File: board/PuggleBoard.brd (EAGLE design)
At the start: 54.6 x 86.4 mm, 133 parts, among them U1 LMP7704, U10 SN65LVDS2, U11 SN65LVDS1, U12 SN65LVDS1, U13 SN65LVDS1, U14 SN65MLVD201D, U15 24C, U2 ADS8331, U3 OPA4209, U4 AD5686, U5 LTM8045, U6 TPS7A3001, U7 TPS7A4901, U8 REF5040, U9 AD8032

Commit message: A few minor changes.
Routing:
- net VDRIVE: track 36.6 -> 45.9 mm
- net SPI4: track 9.88 -> 17.7 mm
- net MISO1_N: track 17.8 -> 19.3 mm
- net MISO1_P: track 21.8 -> 23.2 mm
- net GND: track 115.6 -> 116.4 mm
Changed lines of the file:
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@@
 <layers>
 <layer number="1" name="Top" color="12" fill="1" visible="yes" active="yes"/>
-<layer number="2" name="GND" color="12" fill="3" visible="no" active="yes"/>
+<layer number="2" name="GND" color="12" fill="3" visible="yes" active="yes"/>
 <layer number="3" name="Route3" color="4" fill="3" visible="no" active="no"/>
 <layer number="4" name="Route4" color="1" fill="4" visible="no" active="no"/>
@@
 <layer number="13" name="Route13" color="4" fill="5" visible="no" active="no"/>
 <layer number="14" name="Route14" color="1" fill="6" visible="no" active="no"/>
-<layer number="15" name="PWR" color="1" fill="6" visible="no" active="yes"/>
+<layer number="15" name="PWR" color="1" fill="6" visible="yes" active="yes"/>
 <layer number="16" name="Bottom" color="1" fill="1" visible="yes" active="yes"/>
 <layer number="17" name="Pads" color="10" fill="1" visible="yes" active="yes"/>
@@
 <wire x1="46.609" y1="69.088" x2="46.609" y2="68.06155" width="0.4064" layer="16"/>
 <wire x1="46.609" y1="68.06155" x2="46.86269375" y2="68.06155" width="0.4064" layer="16"/>
+<wire x1="45.847" y1="78.4606" x2="44.2468" y2="76.8604" width="0.4064" layer="16"/>
+<wire x1="44.2468" y1="76.8604" x2="44.2468" y2="76.3016" width="0.4064" layer="16"/>
+<wire x1="45.847" y1="73.2536" x2="44.2468" y2="71.6534" width="0.4064" layer="16"/>
+<wire x1="44.2468" y1="71.6534" x2="44.2468" y2="71.0946" width="0.4064" layer="16"/>
+<wire x1="45.847" y1="68.0466" x2="44.2468" y2="66.4464" width="0.4064" layer="16"/>
+<wire x1="44.2468" y1="66.4464" x2="44.2468" y2="65.8876" width="0.4064" layer="16"/>
+<wire x1="33.274" y1="82.296" x2="34.0995" y2="82.296" width="0.4064" layer="1"/>
 <wire x1="66.3194" y1="55.626" x2="66.3194" y2="57.658" width="0" layer="19" extent="1-1"/>
 <wire x1="68.8848" y1="52.705" x2="66.3194" y2="55.626" width="0" layer="19" extent="1-1"/>
 <wire x1="47.371" y1="68.0466" x2="66.3194" y2="57.658" width="0" layer="19" extent="1-16"/>
 <wire x1="11.5316" y1="8.001" x2="11.684" y2="8.001" width="0" layer="19" extent="1-1"/>
-<wire x1="34.0995" y1="82.296" x2="33.274" y2="82.296" width="0" layer="19" extent="1-1"/>
 <wire x1="37.3126" y1="47.371" x2="38.354" y2="47.371" width="0" layer="19" extent="1-1"/>
-<wire x1="44.2468" y1="76.3016" x2="45.847" y2="78.4606" width="0" layer="19" extent="16-16"/>
-<wire x1="44.2468" y1="71.0946" x2="45.847" y2="73.2536" width="0" layer="19" extent="16-16"/>
-<wire x1="44.2468" y1="65.8876" x2="45.847" y2="68.0466" width="0" layer="19" extent="16-16"/>
 </signal>
 <signal name="VDD_5V">
@@
 <wire x1="42.545" y1="41.785" x2="42.547" y2="41.783" width="1.016" layer="1"/>
 <wire x1="42.547" y1="41.783" x2="44.45" y2="41.783" width="1.016" layer="1"/>
+<wire x1="33.274" y1="81.153" x2="34.0995" y2="81.153" width="0.4064" layer="1"/>
 <wire x1="68.0466" y1="55.626" x2="68.0466" y2="57.658" width="0" layer="19" extent="1-1"/>
 <wire x1="68.8848" y1="48.895" x2="68.0466" y2="55.626" width="0" layer="19" extent="1-1"/>
@@
 <wire x1="26.162" y1="76.4286" x2="26.162" y2="76.327" width="0" layer="19" extent="16-16"/>
 <wire x1="31.1404" y1="52.705" x2="31.242" y2="52.832" width="0" layer="19" extent="16-16"/>
-<wire x1="34.0995" y1="81.153" x2="33.274" y2="81.153" width="0" layer="19" extent="1-1"/>
 </signal>
 <signal name="BAT_SENSE">
@@
 <contactref element="BB1" pad="76"/>
 <wire x1="36.7284" y1="56.642" x2="46.609" y2="56.642" width="0.254" layer="1"/>
+<wire x1="30.3276" y1="58.801" x2="30.3276" y2="58.6994" width="0.254" layer="1"/>
+<wire x1="30.3276" y1="58.6994" x2="30.861" y2="58.166" width="0.254" layer="1"/>
+<wire x1="30.861" y1="58.166" x2="36.068" y2="58.166" width="0.254" layer="1"/>
+<wire x1="36.068" y1="58.166" x2="36.703" y2="57.531" width="0.254" layer="1"/>
+<wire x1="36.703" y1="57.531" x2="36.703" y2="56.6674" width="0.254" layer="1"/>
+<wire x1="36.703" y1="56.6674" x2="36.7284" y2="56.642" width="0.254" layer="1"/>
 <wire x1="46.609" y1="56.642" x2="50.165" y2="54.61" width="0" layer="19" extent="1-1"/>
-<wire x1="30.3276" y1="58.801" x2="36.7284" y2="56.642" width="0" layer="19" extent="1-1"/>
 </signal>
 <signal name="BOARD_TEMP">
@@
 <wire x1="39.3016125" y1="66.8909" x2="40.4495" y2="66.8909" width="0.1778" layer="16"/>
 <wire x1="40.4495" y1="66.8909" x2="41.148" y2="66.1924" width="0.1778" layer="16"/>
-<wire x1="41.148" y1="66.1924" x2="42.3672" y2="65.8876" width="0" layer="19" extent="16-16"/>
+<wire x1="41.148" y1="66.1924" x2="41.1734" y2="66.167" width="0.1778" layer="16"/>
+<wire x1="41.1734" y1="66.167" x2="41.783" y2="66.167" width="0.1778" layer="16"/>
+<wire x1="41.783" y1="66.167" x2="42.0624" y2="65.8876" width="0.1778" layer="16"/>
+<wire x1="42.0624" y1="65.8876" x2="42.3672" y2="65.8876" width="0.1778" layer="16"/>
 </signal>
 <signal name="MISO1_N" class="2">
@@
 <wire x1="39.4383875" y1="67.2211" x2="40.4495" y2="67.2211" width="0.1778" layer="16"/>
 <wire x1="40.4495" y1="67.2211" x2="41.148" y2="67.9196" width="0.1778" layer="16"/>
-<wire x1="41.148" y1="67.9196" x2="42.3672" y2="68.4784" width="0" layer="19" extent="16-16"/>
+<wire x1="41.148" y1="67.9196" x2="41.8084" y2="67.9196" width="0.1778" layer="16"/>
+<wire x1="41.8084" y1="67.9196" x2="42.3672" y2="68.4784" width="0.1778" layer="16"/>
 </signal>
 <signal name="N$8">

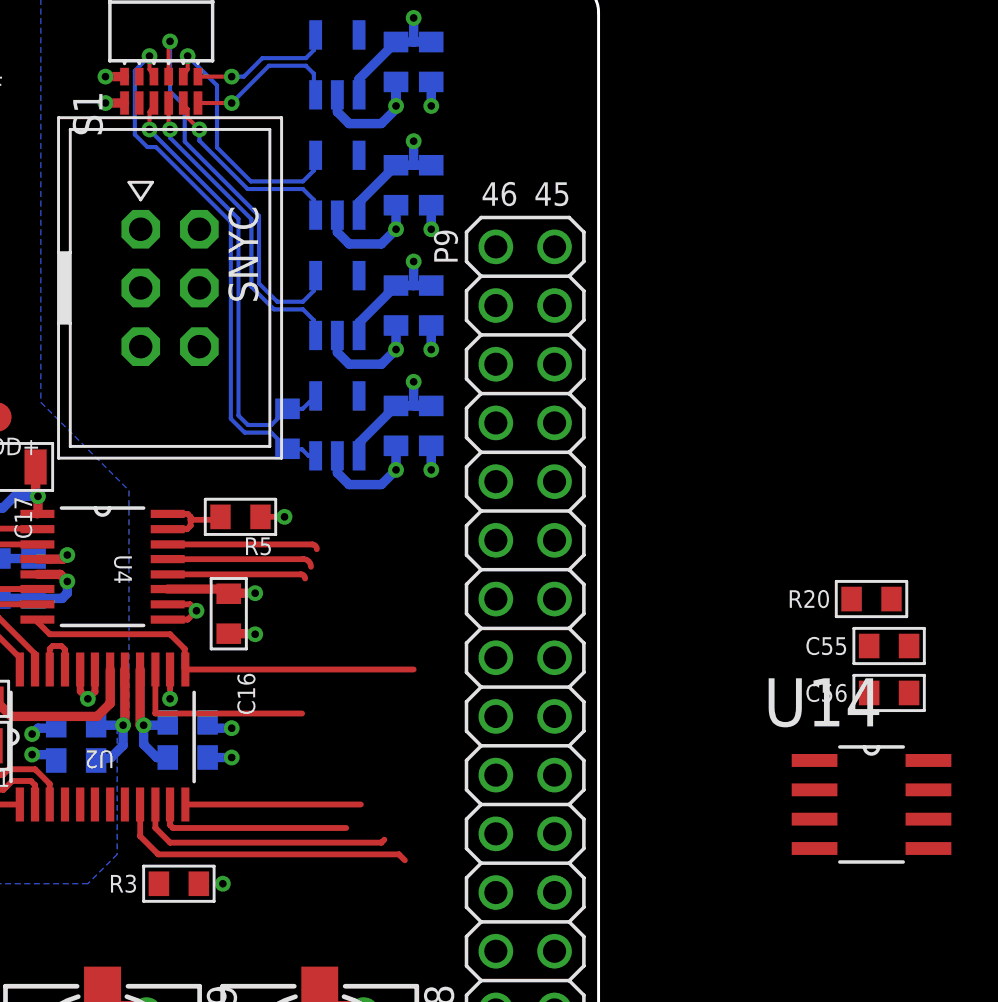
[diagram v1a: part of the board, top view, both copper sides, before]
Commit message: Did some of the differential pair wiring.
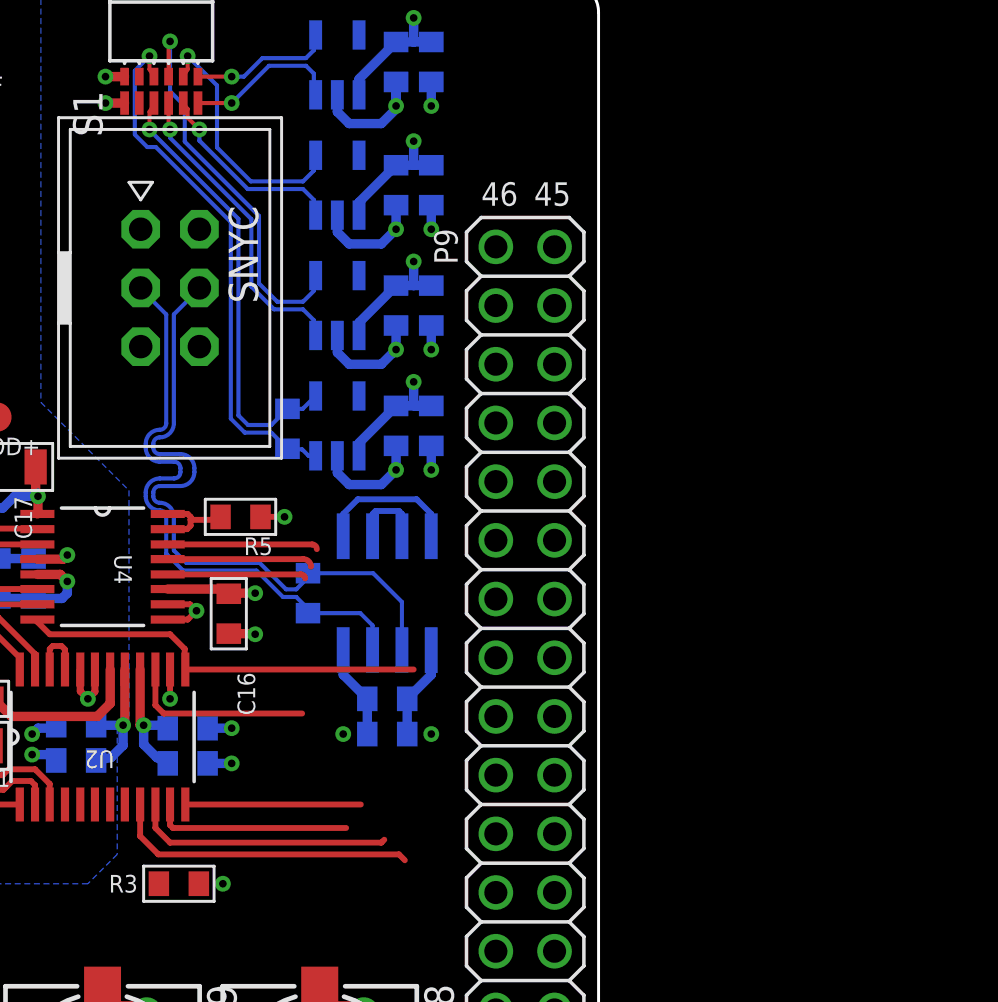
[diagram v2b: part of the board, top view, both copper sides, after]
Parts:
- moved R20 24.4 mm to (42.0, 59.9), flipped to the bottom, turned to 270 degrees
- moved U14 22.9 mm to (45.5, 59.9), flipped to the bottom, turned to 270 degrees
- moved C55 22.0 mm to (45.5, 53.8), flipped to the bottom, turned to 180 degrees
- moved C56 21.7 mm to (45.5, 55.4), flipped to the bottom, turned to 180 degrees
- moved C1 0.25 mm to (36.8, 54.1)
- moved C2 0.25 mm to (36.8, 52.6)
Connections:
- removed net N$11: R20.2, SNYC.4, U14.7
- removed net N$7: R20.1, SNYC.3, U14.6
- new net SYNC_N: R20.2, SNYC.3, U14.7
- new net SYNC_P: R20.1, SNYC.4, U14.6
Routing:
- net SYNC_P: track 0.00 -> 28.6 mm
- net SYNC_N: track 0.00 -> 26.1 mm
- net N$12: track 0.00 -> 6.27 mm
- net VDRIVE: track 45.9 -> 50.1 mm, vias 17 -> 18
- net GND: track 116.4 -> 120.5 mm, vias 85 -> 86
- net N$17: track 0.00 -> 3.31 mm

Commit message: Minor.
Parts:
- moved SNYC 0.64 mm to (36.1, 72.5)
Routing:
- net SYNC_P: track 28.6 -> 28.0 mm
- net SYNC_N: track 26.1 -> 25.4 mm
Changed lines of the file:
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@@
 <attribute name="OC_FARNELL" value="-" x="45.466" y="59.944" size="1.778" layer="28" rot="MR270" display="off"/>
 </element>
-<element name="SNYC" library="puggleboard" package="2X03_IDC" value="PINHD-2X3_IDC" x="36.068" y="73.152" rot="R270"/>
+<element name="SNYC" library="puggleboard" package="2X03_IDC" value="PINHD-2X3_IDC" x="36.068" y="72.517" rot="R270"/>
 <element name="R20" library="puggleboard" package="0603" value="100" x="42.037" y="59.944" rot="MR270">
 <attribute name="MN" value="Panasonic" x="41.91" y="57.785" size="1.778" layer="28" rot="MR270" display="off"/>
@@
 <contactref element="SNYC" pad="3"/>
 <wire x1="42.037" y1="59.0804" x2="44.2976" y2="59.0804" width="0.1778" layer="16"/>
-<wire x1="34.798" y1="73.152" x2="34.798" y2="73.1139" width="0.1778" layer="16"/>
-<wire x1="34.798" y1="73.1139" x2="35.9029" y2="72.009" width="0.1778" layer="16"/>
-<wire x1="35.9029" y1="72.009" x2="35.9029" y2="67.2953" width="0.1778" layer="16"/>
+<wire x1="34.798" y1="72.517" x2="34.798" y2="72.4789" width="0.1778" layer="16"/>
+<wire x1="34.798" y1="72.4789" x2="35.9029" y2="71.374" width="0.1778" layer="16"/>
+<wire x1="35.9029" y1="71.374" x2="35.9029" y2="67.2953" width="0.1778" layer="16"/>
 <wire x1="35.9029" y1="67.2953" x2="35.6235" y2="67.0159" width="0.1778" layer="16" curve="-90"/>
 <wire x1="35.6235" y1="67.0159" x2="35.0139" y2="66.4063" width="0.1778" layer="16" curve="90"/>
@@
 <contactref element="SNYC" pad="4"/>
 <wire x1="42.037" y1="60.8076" x2="44.8564" y2="60.8076" width="0.1778" layer="16"/>
-<wire x1="37.338" y1="73.152" x2="37.338" y2="73.1139" width="0.1778" layer="16"/>
-<wire x1="37.338" y1="73.1139" x2="36.2331" y2="72.009" width="0.1778" layer="16"/>
-<wire x1="36.2331" y1="72.009" x2="36.2331" y2="67.2953" width="0.1778" layer="16"/>
+<wire x1="37.338" y1="72.517" x2="37.338" y2="72.4789" width="0.1778" layer="16"/>
+<wire x1="37.338" y1="72.4789" x2="36.2331" y2="71.374" width="0.1778" layer="16"/>
+<wire x1="36.2331" y1="71.374" x2="36.2331" y2="67.2953" width="0.1778" layer="16"/>
 <wire x1="36.2331" y1="67.2953" x2="35.6235" y2="66.6857" width="0.1778" layer="16" curve="-90"/>
 <wire x1="35.6235" y1="66.6857" x2="35.3441" y2="66.4063" width="0.1778" layer="16" curve="90"/>

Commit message: updated digital lines with new pinout; EEPROM still using pins 19 and 20
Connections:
- removed net N$12: U14.1, U14.4
- removed net N$17: U14.2, U14.3
- new net MS_PIN1: BB1.71, U14.1, U14.4
- new net MS_PIN2: BB1.87, U14.2, U14.3
- net SPI5: now also BB1.73; no longer BB1.78
- net SPI6: now also BB1.70; no longer BB1.73
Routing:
- net N$12: track 6.27 -> 0.00 mm
- net MS_PIN1: track 0.00 -> 6.27 mm
- net N$17: track 3.31 -> 0.00 mm
- net MS_PIN2: track 0.00 -> 3.31 mm
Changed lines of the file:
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@@
 <?xml version="1.0" encoding="utf-8"?>
 <!DOCTYPE eagle SYSTEM "eagle.dtd">
-<eagle version="6.5.0">
+<eagle version="6.4">
 <drawing>
 <settings>
@@
 <signal name="SPI5">
 <contactref element="U2" pad="15"/>
-<contactref element="BB1" pad="78"/>
 <wire x1="35.433" y1="56.642" x2="35.433" y2="55.096209375" width="0.254" layer="1"/>
 <wire x1="35.433" y1="55.096209375" x2="35.792209375" y2="54.737" width="0.254" layer="1"/>
 <wire x1="35.792209375" y1="54.737" x2="41.783" y2="54.737" width="0.254" layer="1"/>
-<wire x1="41.783" y1="54.737" x2="50.165" y2="57.15" width="0" layer="19" extent="1-1"/>
+<contactref element="BB1" pad="73"/>
+<wire x1="41.783" y1="54.737" x2="52.705" y2="52.07" width="0" layer="19" extent="1-1"/>
 </signal>
 <signal name="N$37">
@@
 <signal name="SPI6">
 <contactref element="U2" pad="9"/>
-<contactref element="BB1" pad="73"/>
 <wire x1="34.7726" y1="50.8" x2="34.7726" y2="49.4284" width="0.254" layer="1"/>
 <wire x1="34.7726" y1="49.4284" x2="35.56" y2="48.641" width="0.254" layer="1"/>
 <wire x1="35.56" y1="48.641" x2="45.974" y2="48.641" width="0.254" layer="1"/>
 <wire x1="45.974" y1="48.641" x2="46.228" y2="48.387" width="0.254" layer="1"/>
-<wire x1="46.228" y1="48.387" x2="52.705" y2="52.07" width="0" layer="19" extent="1-1"/>
+<contactref element="BB1" pad="70"/>
+<wire x1="46.228" y1="48.387" x2="50.165" y2="46.99" width="0" layer="19" extent="1-1"/>
 </signal>
 <signal name="SPI10">
@@
 <wire x1="41.529" y1="60.1091" x2="42.037" y2="60.6171" width="0.1778" layer="16"/>
 <wire x1="42.037" y1="60.6171" x2="42.037" y2="60.8076" width="0.1778" layer="16"/>
-</signal>
-<signal name="N$12">
-<contactref element="U14" pad="1"/>
-<contactref element="U14" pad="4"/>
-<wire x1="43.561" y1="62.4078" x2="43.561" y2="63.373" width="0.254" layer="16"/>
-<wire x1="43.561" y1="63.373" x2="44.196" y2="64.008" width="0.254" layer="16"/>
-<wire x1="44.196" y1="64.008" x2="46.736" y2="64.008" width="0.254" layer="16"/>
-<wire x1="46.736" y1="64.008" x2="47.371" y2="63.373" width="0.254" layer="16"/>
-<wire x1="47.371" y1="63.373" x2="47.371" y2="62.4078" width="0.254" layer="16"/>
-</signal>
-<signal name="N$17">
-<contactref element="U14" pad="2"/>
-<contactref element="U14" pad="3"/>
-<wire x1="44.831" y1="62.4078" x2="44.831" y2="63.373" width="0.254" layer="16"/>
-<wire x1="44.831" y1="63.373" x2="44.958" y2="63.5" width="0.254" layer="16"/>
-<wire x1="44.958" y1="63.5" x2="45.974" y2="63.5" width="0.254" layer="16"/>
-<wire x1="45.974" y1="63.5" x2="46.101" y2="63.373" width="0.254" layer="16"/>
-<wire x1="46.101" y1="63.373" x2="46.101" y2="62.4078" width="0.254" layer="16"/>
 </signal>
 <signal name="VSS_POST_LC">
@@
 <wire x1="38.1254" y1="63.119" x2="36.957" y2="63.119" width="0.254" layer="1"/>
 </signal>
+<signal name="MS_PIN2">
+<contactref element="BB1" pad="87"/>
+<contactref element="U14" pad="2"/>
+<contactref element="U14" pad="3"/>
+<wire x1="44.831" y1="62.4078" x2="44.831" y2="63.373" width="0.254" layer="16"/>
+<wire x1="44.831" y1="63.373" x2="44.958" y2="63.5" width="0.254" layer="16"/>
+<wire x1="44.958" y1="63.5" x2="45.974" y2="63.5" width="0.254" layer="16"/>
+<wire x1="45.974" y1="63.5" x2="46.101" y2="63.373" width="0.254" layer="16"/>
+<wire x1="46.101" y1="63.373" x2="46.101" y2="62.4078" width="0.254" layer="16"/>
+<wire x1="46.101" y1="63.373" x2="52.705" y2="69.85" width="0" layer="19" extent="16-16"/>
+</signal>
+<signal name="MS_PIN1">
+<contactref element="BB1" pad="71"/>
+<contactref element="U14" pad="1"/>
+<contactref element="U14" pad="4"/>
+<wire x1="43.561" y1="62.4078" x2="43.561" y2="63.373" width="0.254" layer="16"/>
+<wire x1="43.561" y1="63.373" x2="44.196" y2="64.008" width="0.254" layer="16"/>
+<wire x1="44.196" y1="64.008" x2="46.736" y2="64.008" width="0.254" layer="16"/>
+<wire x1="46.736" y1="64.008" x2="47.371" y2="63.373" width="0.254" layer="16"/>
+<wire x1="47.371" y1="63.373" x2="47.371" y2="62.4078" width="0.254" layer="16"/>
+<wire x1="52.705" y1="49.53" x2="47.371" y2="62.4078" width="0" layer="19" extent="16-16"/>
+</signal>
 </signals>
-<errors>
-</errors>
 </board>
 </drawing>

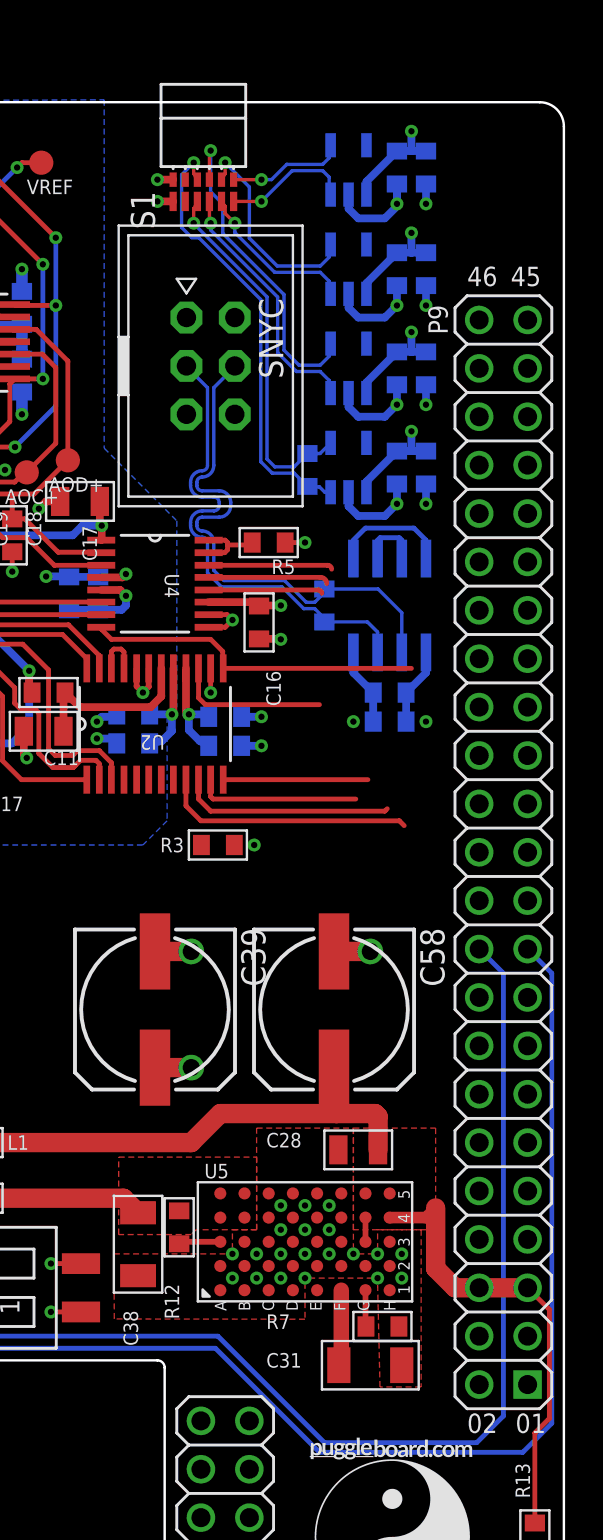
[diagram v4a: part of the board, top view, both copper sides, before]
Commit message: Routing complete. Many ERC and DRC fixes.
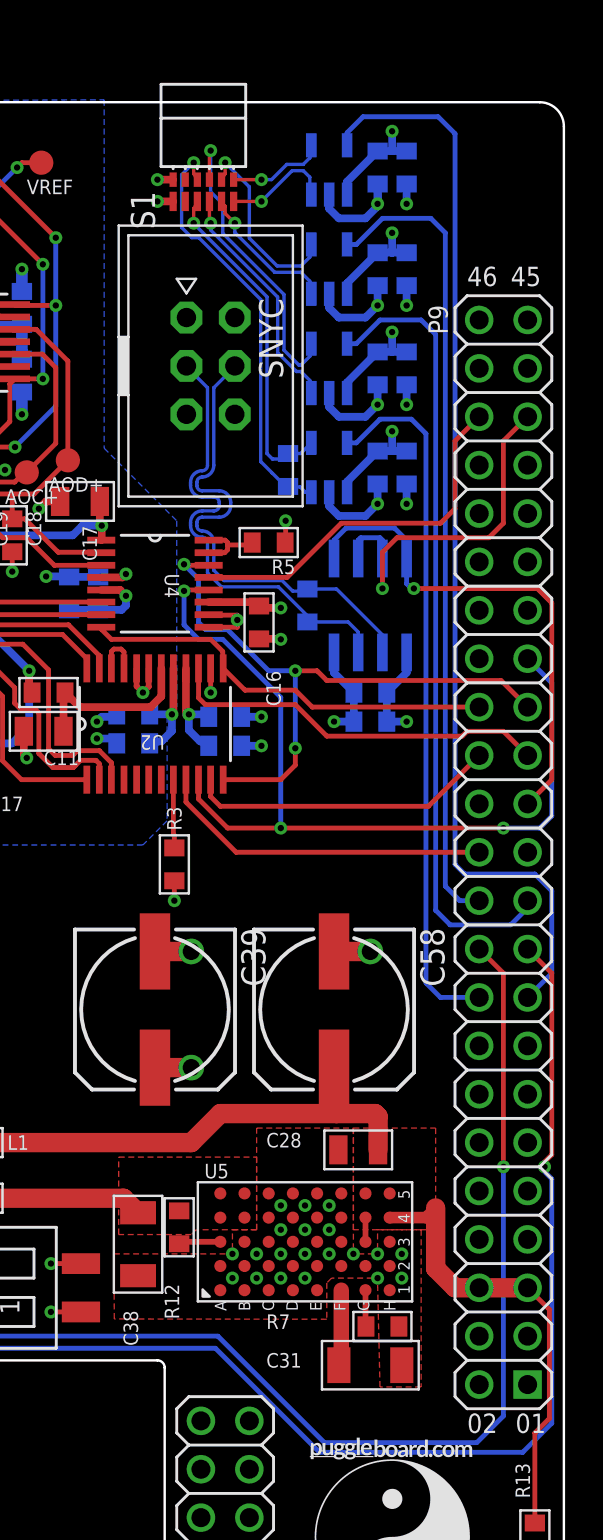
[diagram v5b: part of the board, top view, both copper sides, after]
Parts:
- R20: value 100 -> 150
- moved R3 2.50 mm to (34.2, 46.4), turned to 270 degrees
- moved U$2 1.89 mm to (128.8, 34.8)
- moved C47 1.02 mm to (46.4, 67.2)
- moved C48 1.02 mm to (46.4, 82.9)
- moved C49 1.02 mm to (46.4, 72.4)
- moved C50 1.02 mm to (46.4, 77.6)
- moved R19 1.02 mm to (40.1, 67.1)
- moved U10 1.02 mm to (42.3, 67.2)
- moved U11 1.02 mm to (42.3, 72.4)
- moved U12 1.02 mm to (42.3, 77.6)
- moved U13 1.02 mm to (42.3, 82.8)
- moved C51 1.02 mm to (44.8, 72.4)
- moved C52 1.02 mm to (44.8, 67.2)
- moved C53 1.02 mm to (44.8, 77.6)
- moved C54 1.02 mm to (44.8, 82.9)
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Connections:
- net MS_PIN1 renamed SYNC
- net MS_PIN2 renamed MASTER/SLAVE
- removed net AIN0: BB1.85
- removed net BOARD_TEMP: U8.3
- removed net N$38: U5.E1
- removed net SYS_5V: BB1.53
- net GND: now also U5.E1
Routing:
- net SPI7: track 0.00 -> 57.2 mm
- net SPI8: track 0.00 -> 42.4 mm
- net SPI9: track 0.00 -> 41.6 mm
- net SPI10: track 0.00 -> 36.9 mm
- net SPI2: track 17.3 -> 45.8 mm, vias 0 -> 3
- net SYNC: track 6.27 -> 26.7 mm, vias 0 -> 1
- net SPI3: track 14.1 -> 32.8 mm, vias 0 -> 3
- net MASTER/SLAVE: track 3.31 -> 19.9 mm, vias 0 -> 1
- net SPI1: track 6.33 -> 19.8 mm
- net SPI5: track 8.04 -> 20.3 mm
- net SPI0: track 8.56 -> 16.3 mm
- net SPI6: track 13.3 -> 17.7 mm
- net SPI4: track 17.7 -> 22.1 mm
- net ~ADCRST: track 0.00 -> 3.60 mm
- net VDRIVE: track 50.1 -> 52.3 mm
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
